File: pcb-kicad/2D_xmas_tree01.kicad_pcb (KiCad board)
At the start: 2 copper layers, 97.2 x 99.7 mm, 41 parts, among them J1 ISP, SW1 SW_SPDT, U1 ATTINY25-20SU

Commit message: Replaced 2018 year on a silk with "Merry Xmas"
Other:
- board text added: "From: Alex & Valery"
- board text added: "Merry Xmas"
- board text added: "New Year"
- board text added: "github.com/kasedy"
- board text removed: "2018"
- board text removed: "steff.fun"
- board text removed: "www.designer2k2.at"
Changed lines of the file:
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@@
-(kicad_pcb (version 20171130) (host pcbnew "(5.0.1)-rc2")
+(kicad_pcb (version 20171130) (host pcbnew "(5.1.4)-1")
   (general
     (thickness 1.6)
-    (drawings 33)
+    (drawings 34)
     (tracks 344)
     (zones 0)
@@
   (layers
     (0 F.Cu signal)
-    (31 B.Cu signal)
-    (32 B.Adhes user)
-    (33 F.Adhes user)
-    (34 B.Paste user)
-    (35 F.Paste user)
+    (31 B.Cu signal hide)
+    (32 B.Adhes user hide)
+    (33 F.Adhes user hide)
+    (34 B.Paste user hide)
+    (35 F.Paste user hide)
     (36 B.SilkS user)
     (37 F.SilkS user)
-    (38 B.Mask user)
-    (39 F.Mask user)
-    (40 Dwgs.User user)
-    (41 Cmts.User user)
-    (42 Eco1.User user)
-    (43 Eco2.User user)
+    (38 B.Mask user hide)
+    (39 F.Mask user hide)
+    (40 Dwgs.User user hide)
+    (41 Cmts.User user hide)
+    (42 Eco1.User user hide)
+    (43 Eco2.User user hide)
     (44 Edge.Cuts user)
     (45 Margin user)
-    (46 B.CrtYd user)
-    (47 F.CrtYd user)
-    (48 B.Fab user)
-    (49 F.Fab user)
+    (46 B.CrtYd user hide)
+    (47 F.CrtYd user hide)
+    (48 B.Fab user hide)
+    (49 F.Fab user hide)
   )
   (setup
@@
     (zone_45_only no)
     (trace_min 0.2)
-    (segment_width 0.2)
-    (edge_width 0.15)
     (via_size 0.8)
     (via_drill 0.4)
@@
     (uvia_min_size 0.2)
     (uvia_min_drill 0.1)
+    (edge_width 0.15)
+    (segment_width 0.2)
     (pcb_text_width 0.3)
     (pcb_text_size 1.5 1.5)
@@
     (visible_elements 7FFFFFFF)
     (pcbplotparams
-      (layerselection 0x010fc_ffffffff)
+      (layerselection 0x00030_7ffffffe)
       (usegerberextensions false)
       (usegerberattributes false)
@@
       (xy -6.4132 48.210702) (xy -6.29233 48.255857) (xy -6.274857 48.26) (xy -6.092213 48.205592)) (layer B.Mask) (width 0.01))
   )
-  (gr_text 2018 (at 147.955 110.49) (layer F.SilkS)
+  (gr_text github.com/kasedy (at 114.935 130.175 284) (layer F.SilkS)
     (effects (font (size 1.5 1.5) (thickness 0.3)))
   )
-  (gr_text steff.fun (at 131.445 62.23 45) (layer B.SilkS)
-    (effects (font (size 1.5 1.5) (thickness 0.3)) (justify mirror))
+  (gr_text "From: Alex & Valery" (at 182.44 130.33 81.5) (layer F.SilkS)
+    (effects (font (size 1.5 1.5) (thickness 0.3)))
   )
-  (gr_text steff.fun (at 131.445 62.23 45) (layer F.SilkS)
+  (gr_text "New Year" (at 147.955 110.49) (layer F.SilkS)
     (effects (font (size 1.5 1.5) (thickness 0.3)))
   )
-  (gr_text www.designer2k2.at (at 182.245 129.54 80) (layer B.SilkS)
+  (gr_text "Merry Xmas" (at 147.955 110.49) (layer B.SilkS)
     (effects (font (size 1.5 1.5) (thickness 0.3)) (justify mirror))
   )
-  (gr_text www.designer2k2.at (at 114.935 130.175 103) (layer F.SilkS)
-    (effects (font (size 1.5 1.5) (thickness 0.3)))
+  (gr_text github.com/kasedy (at 182.44 130.33 81) (layer B.SilkS)
+    (effects (font (size 1.5 1.5) (thickness 0.3)) (justify mirror))
+  )
+  (gr_text "From: Alex & Valery" (at 114.935 130.175 283.5) (layer B.SilkS)
+    (effects (font (size 1.5 1.5) (thickness 0.3)) (justify mirror))
   )
   (gr_line (start 118.745 76.2) (end 99.695 97.79) (layer Edge.Cuts) (width 0.15))

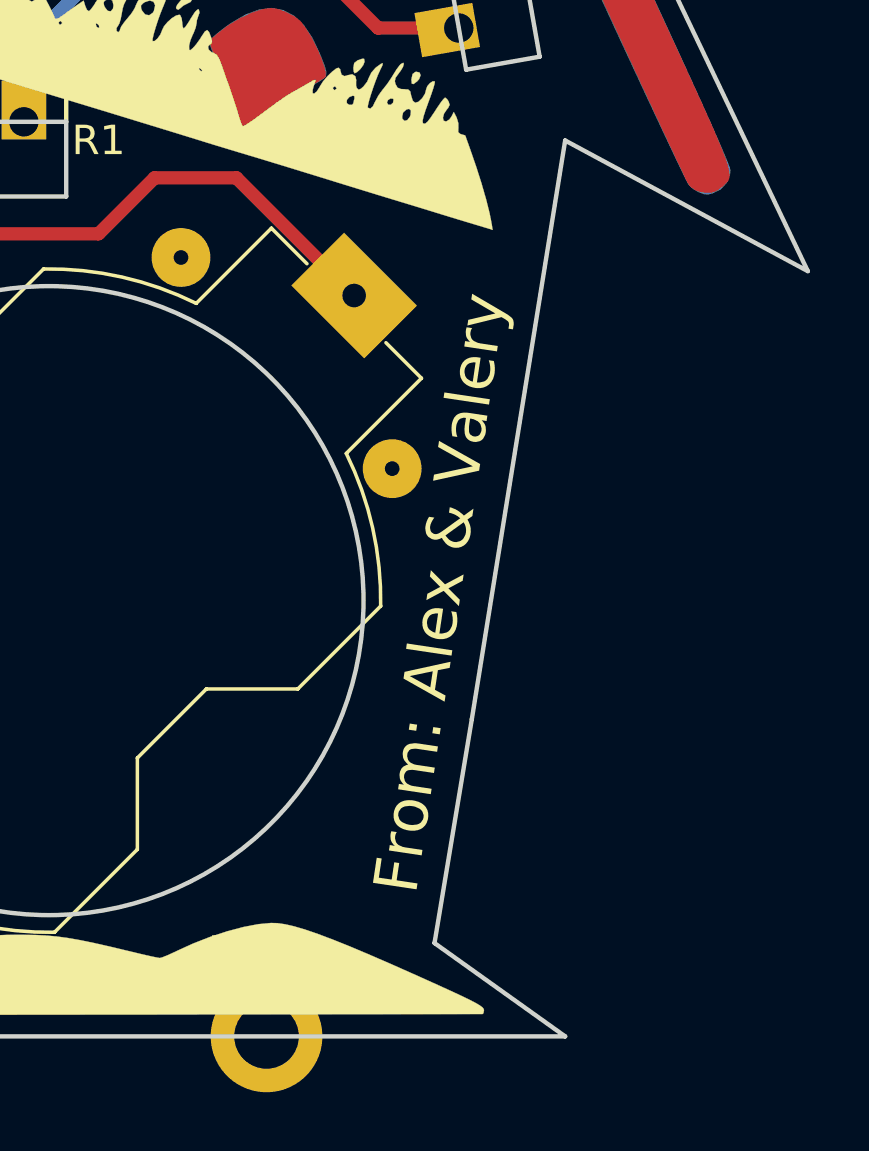
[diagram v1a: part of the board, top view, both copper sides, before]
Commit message: Changed silk layer to include name of the project that anyone who get the pcb know where to find firmware update
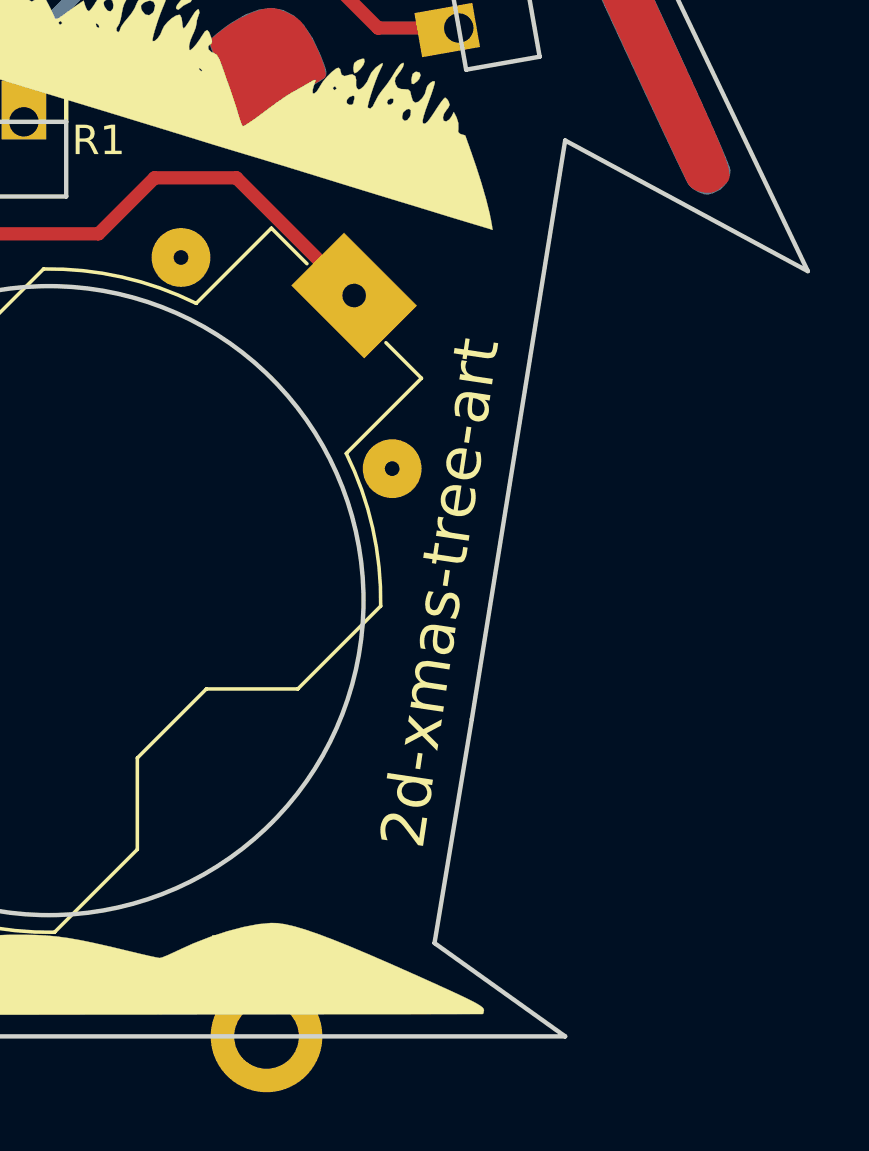
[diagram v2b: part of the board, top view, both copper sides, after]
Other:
- board text added: "2d-xmas-tree-art"
- board text removed: "From: Alex & Valery"
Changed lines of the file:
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@@
     (effects (font (size 1.5 1.5) (thickness 0.3)))
   )
-  (gr_text "From: Alex & Valery" (at 182.44 130.33 81.5) (layer F.SilkS)
+  (gr_text 2d-xmas-tree-art (at 182.44 130.33 81.5) (layer F.SilkS)
     (effects (font (size 1.5 1.5) (thickness 0.3)))
   )
@@
     (effects (font (size 1.5 1.5) (thickness 0.3)) (justify mirror))
   )
-  (gr_text "From: Alex & Valery" (at 114.935 130.175 283.5) (layer B.SilkS)
+  (gr_text 2d-xmas-tree-art (at 114.935 130.175 283.5) (layer B.SilkS)
     (effects (font (size 1.5 1.5) (thickness 0.3)) (justify mirror))
   )

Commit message: Display "From Alex & Valery" of the silk layer of the PCB
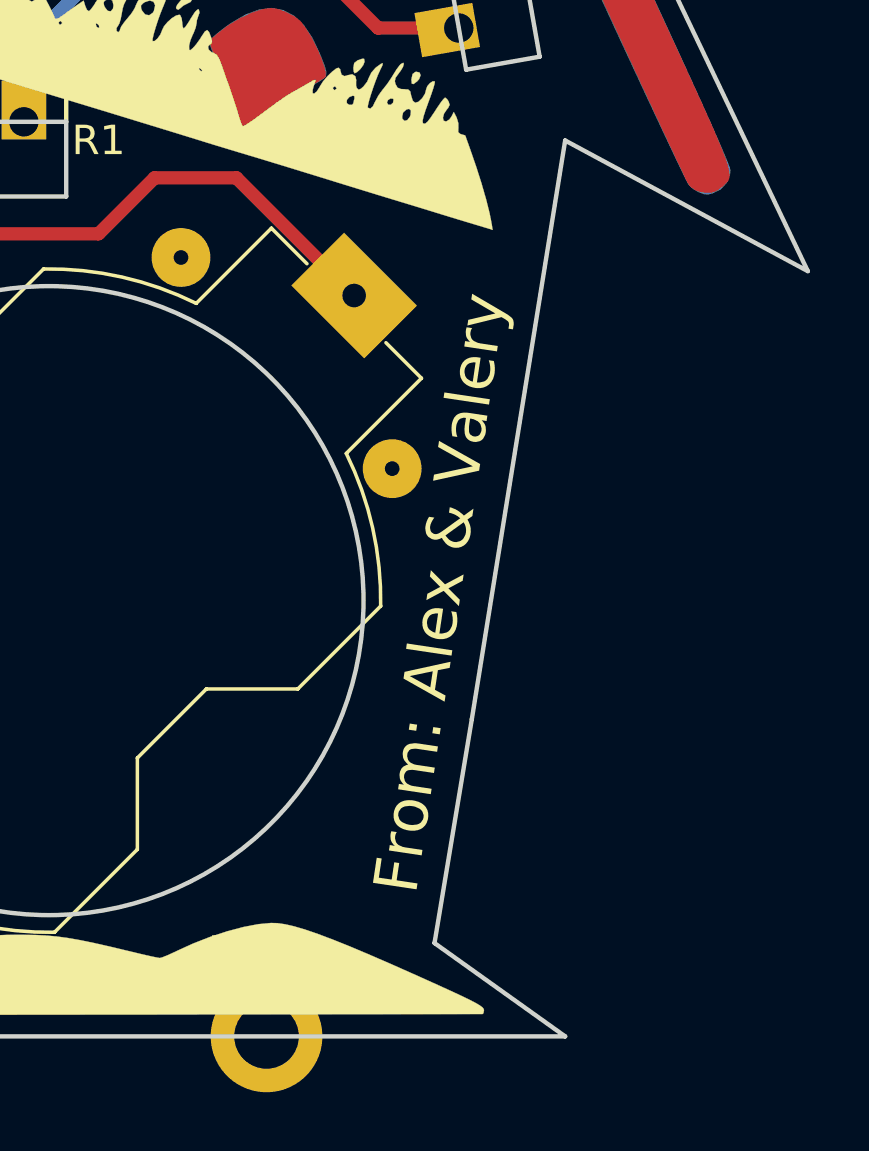
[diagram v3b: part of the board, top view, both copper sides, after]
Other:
- board text added: "From: Alex & Valery"
- board text removed: "2d-xmas-tree-art"
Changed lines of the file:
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@@
     (effects (font (size 1.5 1.5) (thickness 0.3)))
   )
-  (gr_text 2d-xmas-tree-art (at 182.44 130.33 81.5) (layer F.SilkS)
+  (gr_text "From: Alex & Valery" (at 182.44 130.33 81.5) (layer F.SilkS)
     (effects (font (size 1.5 1.5) (thickness 0.3)))
   )
@@
     (effects (font (size 1.5 1.5) (thickness 0.3)) (justify mirror))
   )
-  (gr_text 2d-xmas-tree-art (at 114.935 130.175 283.5) (layer B.SilkS)
+  (gr_text "From: Alex & Valery" (at 114.935 130.175 283.5) (layer B.SilkS)
     (effects (font (size 1.5 1.5) (thickness 0.3)) (justify mirror))
   )
